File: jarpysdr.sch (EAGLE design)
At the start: 37 parts, among them IC1 74HC74N, IC2 NE5532N, IC3 7805, IC4 TL072P

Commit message: Double-sided layout.
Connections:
- net GND: now also J$1.GND@2, J$1.GND@3
- net N$8: now also U1.LEFT; no longer U1.RIGHT
- net N$9: now also U1.RIGHT; no longer U1.LEFT
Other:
- moved on the sheet: U1
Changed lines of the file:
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@@
 <instance part="SUPPLY6" gate="GND" x="149.86" y="86.36"/>
 <instance part="SUPPLY13" gate="GND" x="60.96" y="63.5"/>
-<instance part="SUPPLY17" gate="GND" x="213.36" y="30.48"/>
+<instance part="SUPPLY17" gate="GND" x="215.9" y="30.48"/>
 <instance part="C10" gate="G$1" x="58.42" y="104.14"/>
 <instance part="C8" gate="G$1" x="203.2" y="78.74" rot="R90"/>
@@
 <instance part="SUPPLY21" gate="GND" x="2.54" y="43.18"/>
 <instance part="J$1" gate="1" x="58.42" y="114.3" rot="R270"/>
-<instance part="U1" gate="G$1" x="220.98" y="40.64" rot="R180"/>
+<instance part="U1" gate="G$1" x="223.52" y="43.18" rot="MR0"/>
 </instances>
 <busses>
@@
 <pinref part="SUPPLY12" gate="GND" pin="GND"/>
 <wire x1="43.18" y1="93.98" x2="43.18" y2="119.38" width="0.1524" layer="91"/>
-<wire x1="50.8" y1="119.38" x2="43.18" y2="119.38" width="0.1524" layer="91"/>
+<wire x1="50.8" y1="119.38" x2="48.26" y2="119.38" width="0.1524" layer="91"/>
 <pinref part="J$1" gate="1" pin="GND@1"/>
+<wire x1="48.26" y1="119.38" x2="45.72" y2="119.38" width="0.1524" layer="91"/>
+<wire x1="45.72" y1="119.38" x2="43.18" y2="119.38" width="0.1524" layer="91"/>
 <wire x1="50.8" y1="119.38" x2="50.8" y2="116.84" width="0.1524" layer="91"/>
 <pinref part="J$1" gate="1" pin="GND@0"/>
@@
 <wire x1="53.34" y1="119.38" x2="50.8" y2="119.38" width="0.1524" layer="91"/>
 <junction x="50.8" y="119.38"/>
+<pinref part="J$1" gate="1" pin="GND@2"/>
+<wire x1="48.26" y1="116.84" x2="48.26" y2="119.38" width="0.1524" layer="91"/>
+<pinref part="J$1" gate="1" pin="GND@3"/>
+<wire x1="45.72" y1="116.84" x2="45.72" y2="119.38" width="0.1524" layer="91"/>
+<junction x="45.72" y="119.38"/>
+<junction x="48.26" y="119.38"/>
 </segment>
 <segment>
@@
 </segment>
 <segment>
+<pinref part="SUPPLY17" gate="GND" pin="GND"/>
+<wire x1="215.9" y1="45.72" x2="215.9" y2="33.02" width="0.1524" layer="91"/>
 <pinref part="U1" gate="G$1" pin="SLEEVE"/>
-<pinref part="SUPPLY17" gate="GND" pin="GND"/>
-<wire x1="215.9" y1="38.1" x2="213.36" y2="38.1" width="0.1524" layer="91"/>
-<wire x1="213.36" y1="38.1" x2="213.36" y2="33.02" width="0.1524" layer="91"/>
+<wire x1="218.44" y1="45.72" x2="215.9" y2="45.72" width="0.1524" layer="91"/>
 </segment>
 </net>
@@
 </segment>
 </net>
-<net name="N$8" class="0">
-<segment>
-<pinref part="C11" gate="G$1" pin="2"/>
-<pinref part="U1" gate="G$1" pin="RIGHT"/>
-<wire x1="208.28" y1="40.64" x2="215.9" y2="40.64" width="0.1524" layer="91"/>
-</segment>
-</net>
 <net name="N$9" class="0">
 <segment>
@@
 <wire x1="208.28" y1="78.74" x2="213.36" y2="78.74" width="0.1524" layer="91"/>
 <wire x1="213.36" y1="78.74" x2="213.36" y2="43.18" width="0.1524" layer="91"/>
+<pinref part="U1" gate="G$1" pin="RIGHT"/>
+<wire x1="213.36" y1="43.18" x2="218.44" y2="43.18" width="0.1524" layer="91"/>
+</segment>
+</net>
+<net name="N$8" class="0">
+<segment>
 <pinref part="U1" gate="G$1" pin="LEFT"/>
-<wire x1="213.36" y1="43.18" x2="215.9" y2="43.18" width="0.1524" layer="91"/>
-</segment>
-</net>
+<pinref part="C11" gate="G$1" pin="2"/>
+<wire x1="218.44" y1="40.64" x2="208.28" y2="40.64" width="0.1524" layer="91"/>
+</segment>
+</net>

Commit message: Really-truly final version for release. Sent to fab. Yay.
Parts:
- COUNTER: value 74HC74N -> 74HC74
- DIFF_AMP: value NE5532N -> NE5532
- JP1: value M10" -> Si570
- OUT_AMP: value TL072P -> TL072
- SWITCH: value 74HC4052DIP -> 74HC4052
- VEE-IN: value (none) -> -12v
- renumbered IC1 to COUNTER, IC2 to DIFF_AMP, IC3 to REG-5V, IC4 to OUT_AMP, J$1 to ANTENNA, U$1 to SWITCH

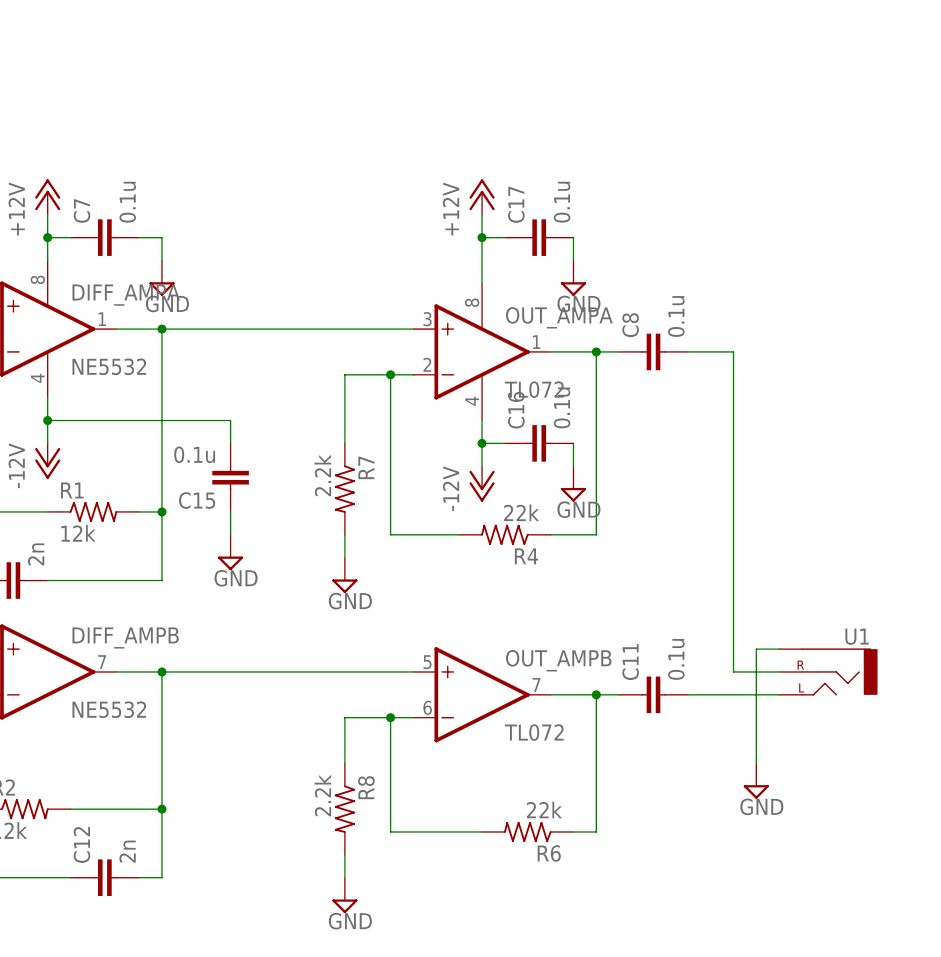
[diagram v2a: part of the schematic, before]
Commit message: AC couple the two opamp stages.
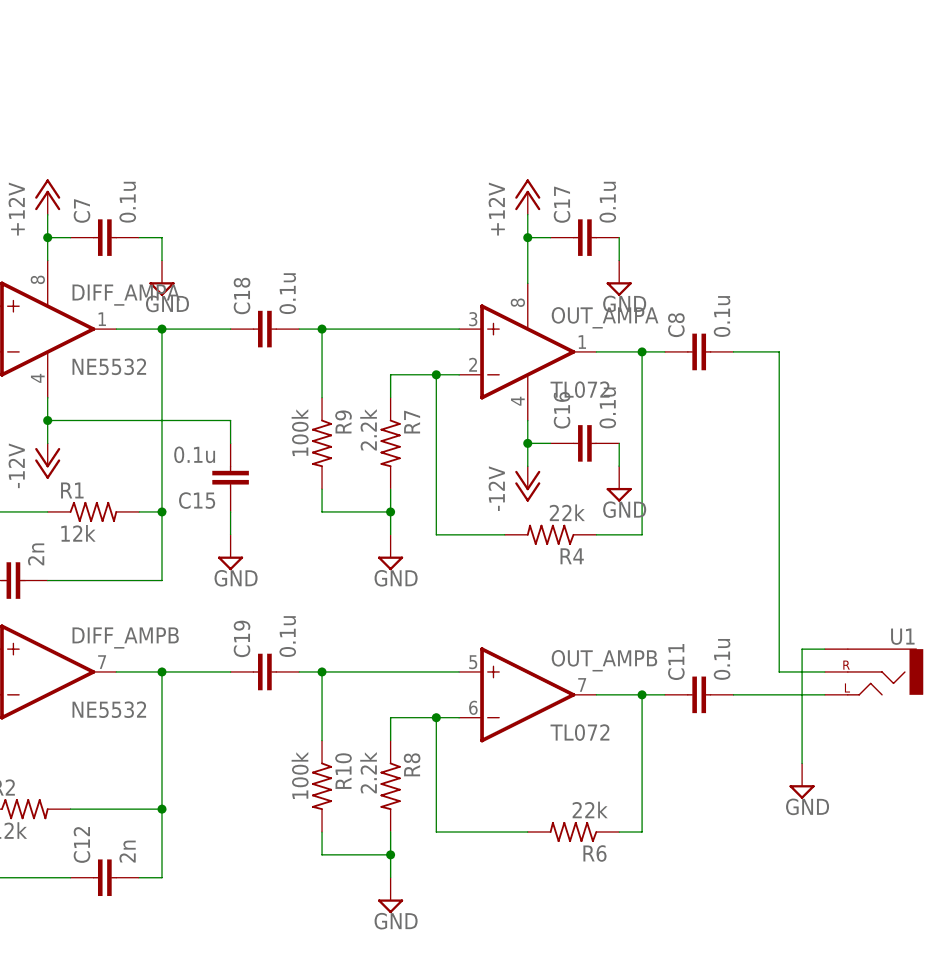
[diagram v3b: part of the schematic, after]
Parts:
- added C18, C19: 0.1u, resistor:C-EU025-025X050
- added R10: 100k, resistor:R-US_0204/7
- added R9: 100k, resistor:R-US_0207/2V
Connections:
- new net N$18: C18.2, OUT_AMPA.+IN, R9.1
- new net N$19: C19.2, OUT_AMPB.+IN, R10.1
- net GND: now also R10.2, R9.2
- net N$10: now also C19.1; no longer OUT_AMPB.+IN
- net N$6: now also C18.1; no longer OUT_AMPA.+IN
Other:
- moved on the sheet: C11, C16, C17, C8, OUT_AMPA, OUT_AMPB, R4, R6, R7, R8, U1

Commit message: - Increased final stage gain. - Increased bandwidth (smaller sampling capacitors).
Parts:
- C0, C1, C2, C3: value 22n -> 15n
- R10, R9: value 100k -> 10k
- R4, R6: value 22k -> 120k
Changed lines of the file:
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@@
 <part name="R1" library="resistor" deviceset="R-US_" device="0207/2V" value="12k"/>
 <part name="R2" library="resistor" deviceset="R-US_" device="0207/2V" value="12k"/>
-<part name="C0" library="resistor" deviceset="C-EU" device="025-024X044" value="22n"/>
-<part name="C1" library="resistor" deviceset="C-EU" device="025-024X044" value="22n"/>
-<part name="C2" library="resistor" deviceset="C-EU" device="025-024X044" value="22n"/>
-<part name="C3" library="resistor" deviceset="C-EU" device="025-024X044" value="22n"/>
+<part name="C0" library="resistor" deviceset="C-EU" device="025-024X044" value="15n"/>
+<part name="C1" library="resistor" deviceset="C-EU" device="025-024X044" value="15n"/>
+<part name="C2" library="resistor" deviceset="C-EU" device="025-024X044" value="15n"/>
+<part name="C3" library="resistor" deviceset="C-EU" device="025-024X044" value="15n"/>
 <part name="SUPPLY5" library="supply2" deviceset="GND" device=""/>
 <part name="SUPPLY8" library="supply2" deviceset="GND" device=""/>
@@
 <part name="SUPPLY3" library="supply2" deviceset="GND" device=""/>
 <part name="OUT_AMP" library="linear" deviceset="TL072" device="P" value="TL072"/>
-<part name="R4" library="resistor" deviceset="R-US_" device="0207/2V" value="22k"/>
+<part name="R4" library="resistor" deviceset="R-US_" device="0207/2V" value="120k"/>
 <part name="P+2" library="supply1" deviceset="+12V" device=""/>
 <part name="P-3" library="supply1" deviceset="-12V" device=""/>
-<part name="R6" library="resistor" deviceset="R-US_" device="0207/2V" value="22k"/>
+<part name="R6" library="resistor" deviceset="R-US_" device="0207/2V" value="120k"/>
 <part name="R7" library="resistor" deviceset="R-US_" device="0207/2V" value="2.2k"/>
 <part name="R8" library="resistor" deviceset="R-US_" device="0204/7" value="2.2k"/>
@@
 <part name="C18" library="resistor" deviceset="C-EU" device="025-025X050" value="0.1u"/>
 <part name="C19" library="resistor" deviceset="C-EU" device="025-025X050" value="0.1u"/>
-<part name="R9" library="resistor" deviceset="R-US_" device="0207/2V" value="100k"/>
-<part name="R10" library="resistor" deviceset="R-US_" device="0204/7" value="100k"/>
+<part name="R9" library="resistor" deviceset="R-US_" device="0207/2V" value="10k"/>
+<part name="R10" library="resistor" deviceset="R-US_" device="0204/7" value="10k"/>
 </parts>
 <sheets>

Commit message: Physical layout for inter-stage AC coupling.
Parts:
- C11, C8: device resistor:C-EU050-045X075 -> resistor:C-EU050-025X075
- C18, C19: device resistor:C-EU025-025X050 -> resistor:C-EU050-025X075
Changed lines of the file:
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@@
 <part name="SUPPLY17" library="supply2" deviceset="GND" device=""/>
 <part name="C10" library="resistor" deviceset="C-EU" device="025-024X044" value="0.1u"/>
-<part name="C8" library="resistor" deviceset="C-EU" device="050-045X075" value="0.1u"/>
-<part name="C11" library="resistor" deviceset="C-EU" device="050-045X075" value="0.1u"/>
+<part name="C8" library="resistor" deviceset="C-EU" device="050-025X075" value="0.1u"/>
+<part name="C11" library="resistor" deviceset="C-EU" device="050-025X075" value="0.1u"/>
 <part name="R3" library="resistor" deviceset="R-US_" device="0204/7" value="2.2k"/>
 <part name="C12" library="resistor" deviceset="C-EU" device="025-024X044" value="2n"/>
@@
 <part name="ANTENNA" library="SparkFun" deviceset="SMA_EDGE" device=""/>
 <part name="U1" library="SparkFun" deviceset="AUDIO-JACK" device="PTH"/>
-<part name="C18" library="resistor" deviceset="C-EU" device="025-025X050" value="0.1u"/>
-<part name="C19" library="resistor" deviceset="C-EU" device="025-025X050" value="0.1u"/>
+<part name="C18" library="resistor" deviceset="C-EU" device="050-025X075" value="0.1u"/>
+<part name="C19" library="resistor" deviceset="C-EU" device="050-025X075" value="0.1u"/>
 <part name="R9" library="resistor" deviceset="R-US_" device="0207/2V" value="10k"/>
 <part name="R10" library="resistor" deviceset="R-US_" device="0204/7" value="10k"/>

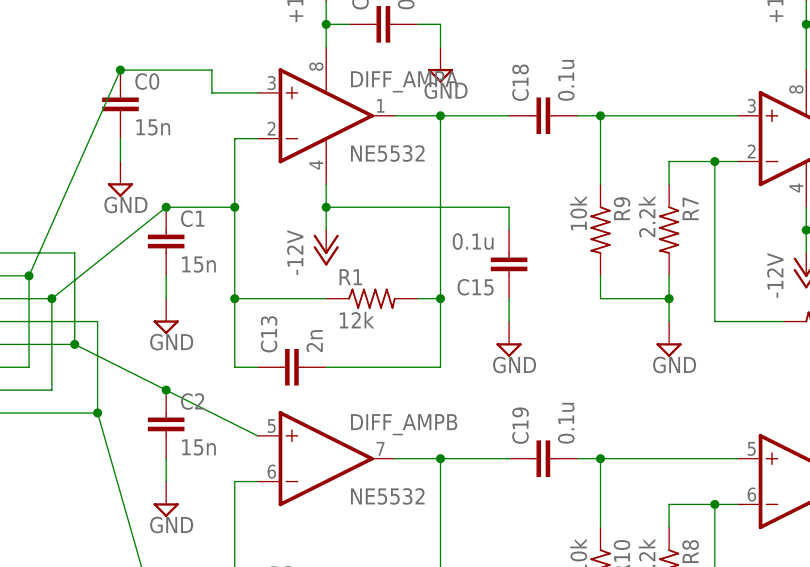
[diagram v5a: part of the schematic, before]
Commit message: Put NE5532 differential amplifier on a single supply.
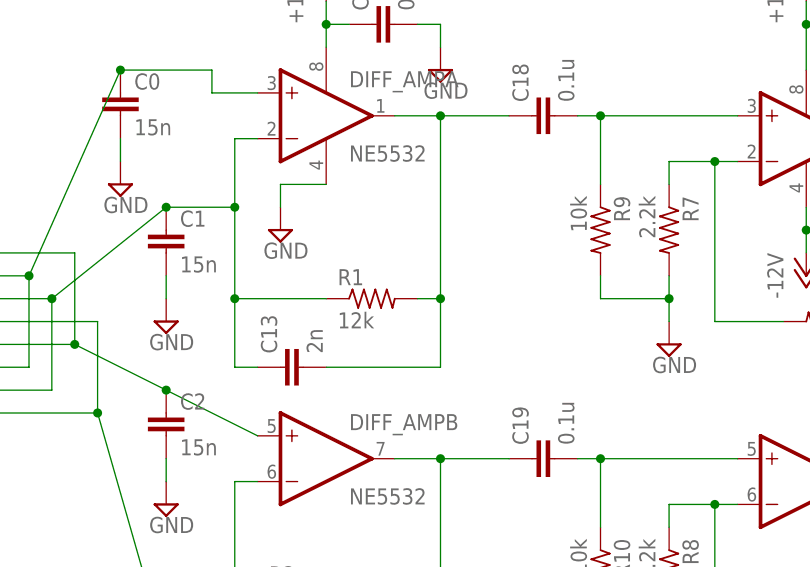
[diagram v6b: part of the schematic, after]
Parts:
- removed C15: 0.1u, resistor:C-EU025-025X050
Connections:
- net -12V: no longer C15.2, DIFF_AMPP.V-
- net GND: now also DIFF_AMPP.V-; no longer C15.1
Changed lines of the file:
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@@
 <part name="C12" library="resistor" deviceset="C-EU" device="025-024X044" value="2n"/>
 <part name="C13" library="resistor" deviceset="C-EU" device="025-024X044" value="2n"/>
-<part name="P-1" library="supply1" deviceset="-12V" device=""/>
 <part name="P-2" library="supply1" deviceset="-12V" device=""/>
 <part name="VEE-IN" library="SparkFun" deviceset="JUMPER-2" device="PTH" value="-12v"/>
 <part name="SUPPLY14" library="supply2" deviceset="GND" device=""/>
 <part name="C14" library="resistor" deviceset="CPOL-EU" device="E2.5-6" value="10u"/>
-<part name="C15" library="resistor" deviceset="C-EU" device="025-025X050" value="0.1u"/>
 <part name="SUPPLY3" library="supply2" deviceset="GND" device=""/>
 <part name="OUT_AMP" library="linear" deviceset="TL072" device="P" value="TL072"/>
@@
 <instance part="C12" gate="G$1" x="142.24" y="20.32" rot="R90"/>
 <instance part="C13" gate="G$1" x="132.08" y="53.34" rot="R90"/>
-<instance part="P-1" gate="1" x="137.16" y="66.04"/>
 <instance part="P-2" gate="1" x="-35.56" y="93.98"/>
 <instance part="VEE-IN" gate="A" x="-33.02" y="106.68"/>
 <instance part="SUPPLY14" gate="GND" x="-27.94" y="93.98"/>
 <instance part="C14" gate="G$1" x="-30.48" y="101.6" rot="R270"/>
-<instance part="C15" gate="G$1" x="157.48" y="63.5" rot="R180"/>
-<instance part="SUPPLY3" gate="GND" x="157.48" y="55.88"/>
+<instance part="SUPPLY3" gate="GND" x="132.08" y="68.58"/>
 <instance part="OUT_AMP" gate="A" x="190.5" y="78.74"/>
 <instance part="OUT_AMP" gate="B" x="190.5" y="40.64"/>
@@
 </segment>
 <segment>
-<wire x1="157.48" y1="60.96" x2="157.48" y2="58.42" width="0.1524" layer="91"/>
-<pinref part="C15" gate="G$1" pin="1"/>
-<pinref part="SUPPLY3" gate="GND" pin="GND"/>
-</segment>
-<segment>
 <wire x1="175.26" y1="58.42" x2="175.26" y2="60.96" width="0.1524" layer="91"/>
 <pinref part="R7" gate="G$1" pin="2"/>
@@
 <pinref part="U1" gate="G$1" pin="SLEEVE"/>
 <wire x1="223.52" y1="45.72" x2="220.98" y2="45.72" width="0.1524" layer="91"/>
+</segment>
+<segment>
+<pinref part="DIFF_AMP" gate="P" pin="V-"/>
+<pinref part="SUPPLY3" gate="GND" pin="GND"/>
+<wire x1="137.16" y1="73.66" x2="132.08" y2="73.66" width="0.1524" layer="91"/>
+<wire x1="132.08" y1="73.66" x2="132.08" y2="71.12" width="0.1524" layer="91"/>
 </segment>
 </net>
@@
 <net name="-12V" class="0">
 <segment>
-<wire x1="137.16" y1="73.66" x2="137.16" y2="71.12" width="0.1524" layer="91"/>
-<wire x1="137.16" y1="71.12" x2="137.16" y2="68.58" width="0.1524" layer="91"/>
-<wire x1="157.48" y1="68.58" x2="157.48" y2="71.12" width="0.1524" layer="91"/>
-<wire x1="157.48" y1="71.12" x2="137.16" y2="71.12" width="0.1524" layer="91"/>
-<junction x="137.16" y="71.12"/>
-<pinref part="DIFF_AMP" gate="P" pin="V-"/>
-<pinref part="P-1" gate="1" pin="-12V"/>
-<pinref part="C15" gate="G$1" pin="2"/>
-</segment>
-<segment>
 <wire x1="-33.02" y1="104.14" x2="-35.56" y2="104.14" width="0.1524" layer="91"/>
